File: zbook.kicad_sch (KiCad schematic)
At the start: 0 parts

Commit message: chore: adds new sheet and removes .lck
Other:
- sheet Peripherals renamed Peripherals 1
- added sheet Peripherals 2 (peripherals2.kicad_sch)
- sheet Peripherals 1: file peripherals.kicad_sch -> peripherals1.kicad_sch
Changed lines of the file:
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@@
 			(color 0 0 0 0.0000)
 		)
-		(property "Sheetname" "Peripherals"
+		(property "Sheetname" "Peripherals 1"
 			(at 138.43 56.4384 0)
 			(effects
@@
 			)
 		)
-		(property "Sheetfile" "peripherals.kicad_sch"
+		(property "Sheetfile" "peripherals1.kicad_sch"
 			(at 138.43 79.3246 0)
 			(effects
@@
 				)
 			)
+		)
+	)
+	(sheet
+		(at 189.23 58.42)
+		(size 19.05 19.05)
+		(exclude_from_sim no)
+		(in_bom yes)
+		(on_board yes)
+		(dnp no)
+		(fields_autoplaced yes)
+		(stroke
+			(width 0.1524)
+			(type solid)
+		)
+		(fill
+			(color 0 0 0 0.0000)
+		)
+		(property "Sheetname" "Peripherals 2"
+			(at 189.23 57.7084 0)
+			(effects
+				(font
+					(size 1.27 1.27)
+				)
+				(justify left bottom)
+			)
+		)
+		(property "Sheetfile" "peripherals2.kicad_sch"
+			(at 189.23 78.0546 0)
+			(effects
+				(font
+					(size 1.27 1.27)
+				)
+				(justify left top)
+			)
+		)
+		(instances
+			(project "zbook"
+				(path "/b90666d0-8852-4bb1-832d-f9d855027372"
+					(page "5")
+				)
+			)

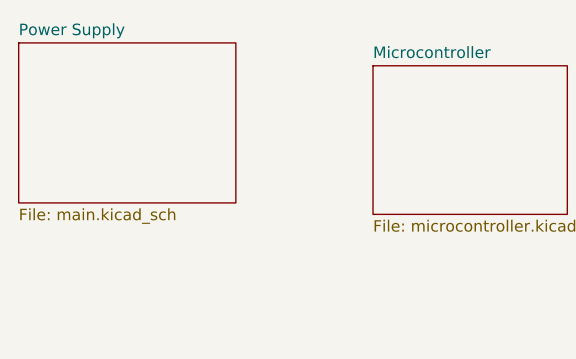
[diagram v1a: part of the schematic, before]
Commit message: refac: changes resistor symbol to US pattern, adds second USB-C connector
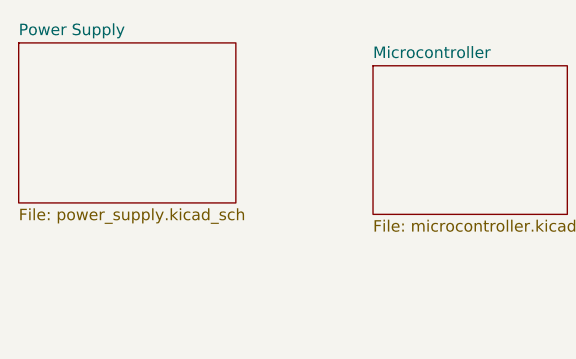
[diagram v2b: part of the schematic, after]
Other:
- sheet Power Supply: file main.kicad_sch -> power_supply.kicad_sch
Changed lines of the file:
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@@
 			)
 		)
-		(property "Sheetfile" "main.kicad_sch"
+		(property "Sheetfile" "power_supply.kicad_sch"
 			(at 44.45 66.6246 0)
 			(effects

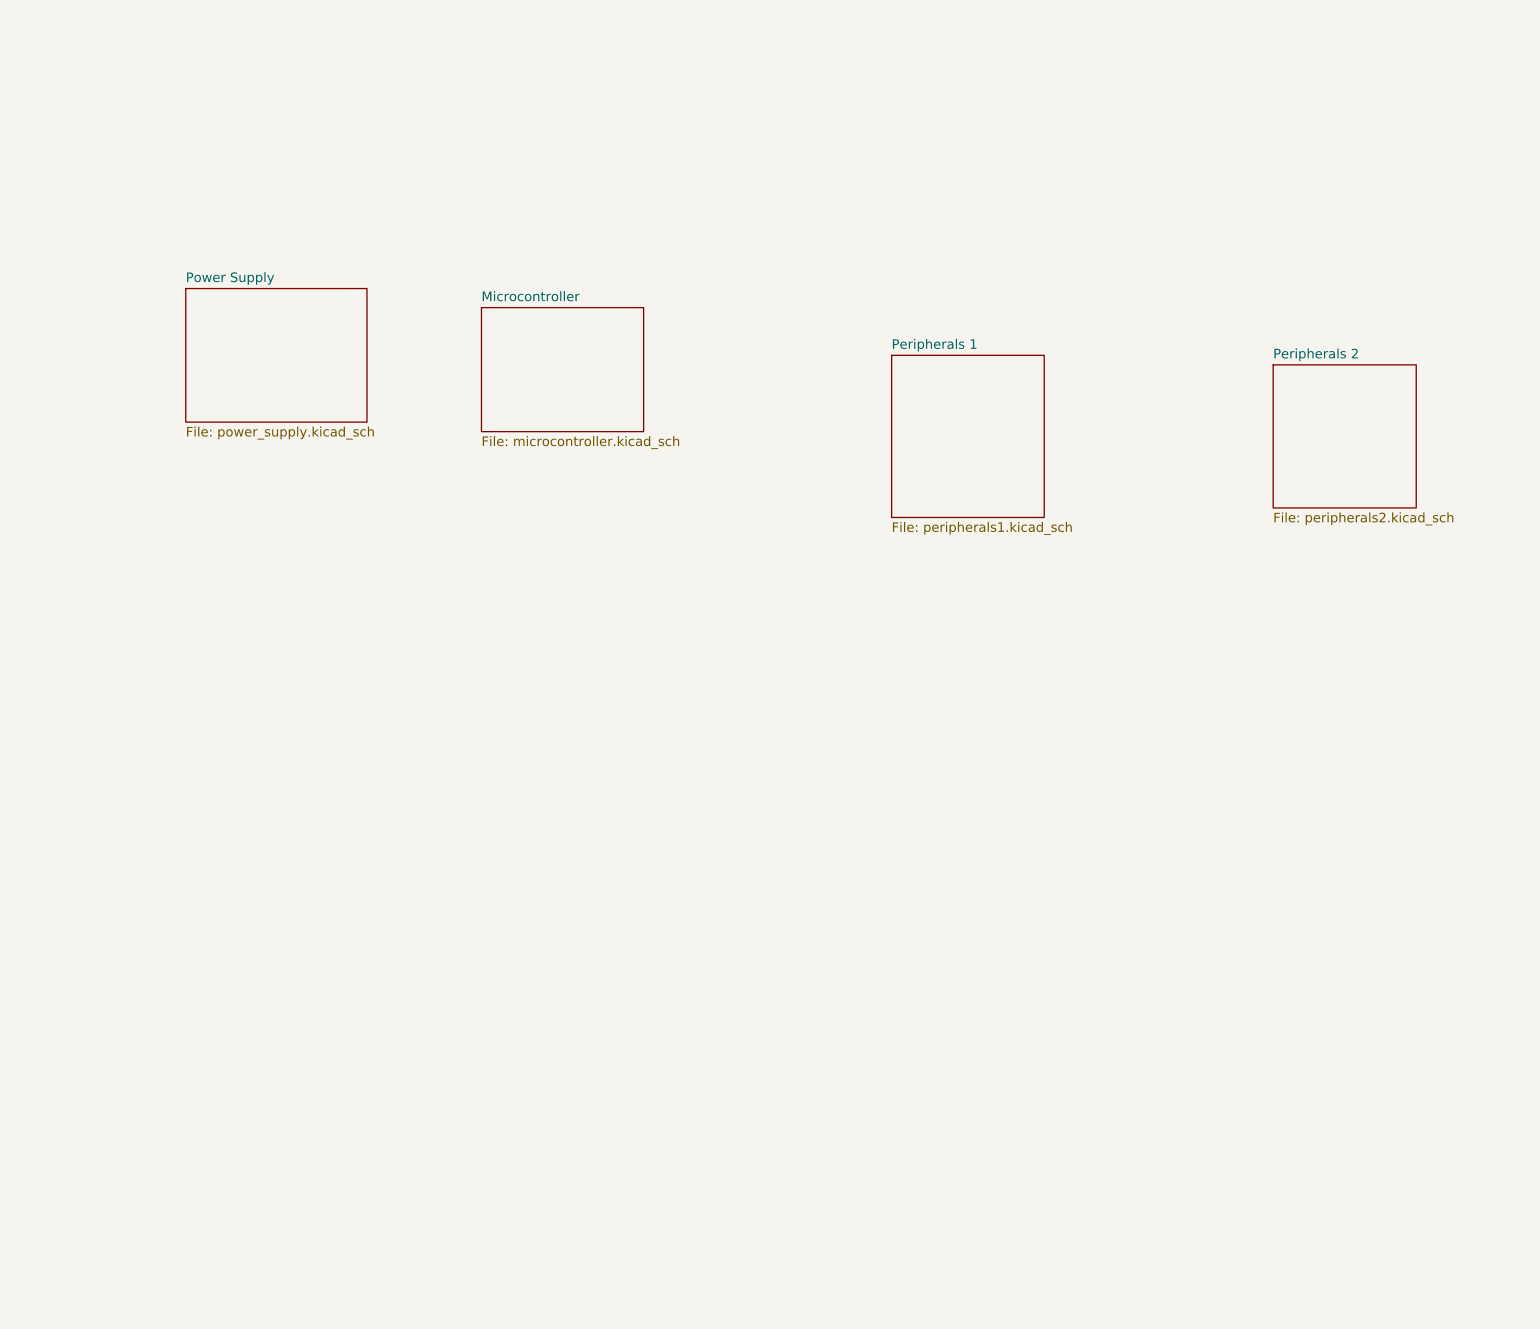
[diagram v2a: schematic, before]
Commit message: chore: adds titles to sheets and organizes root
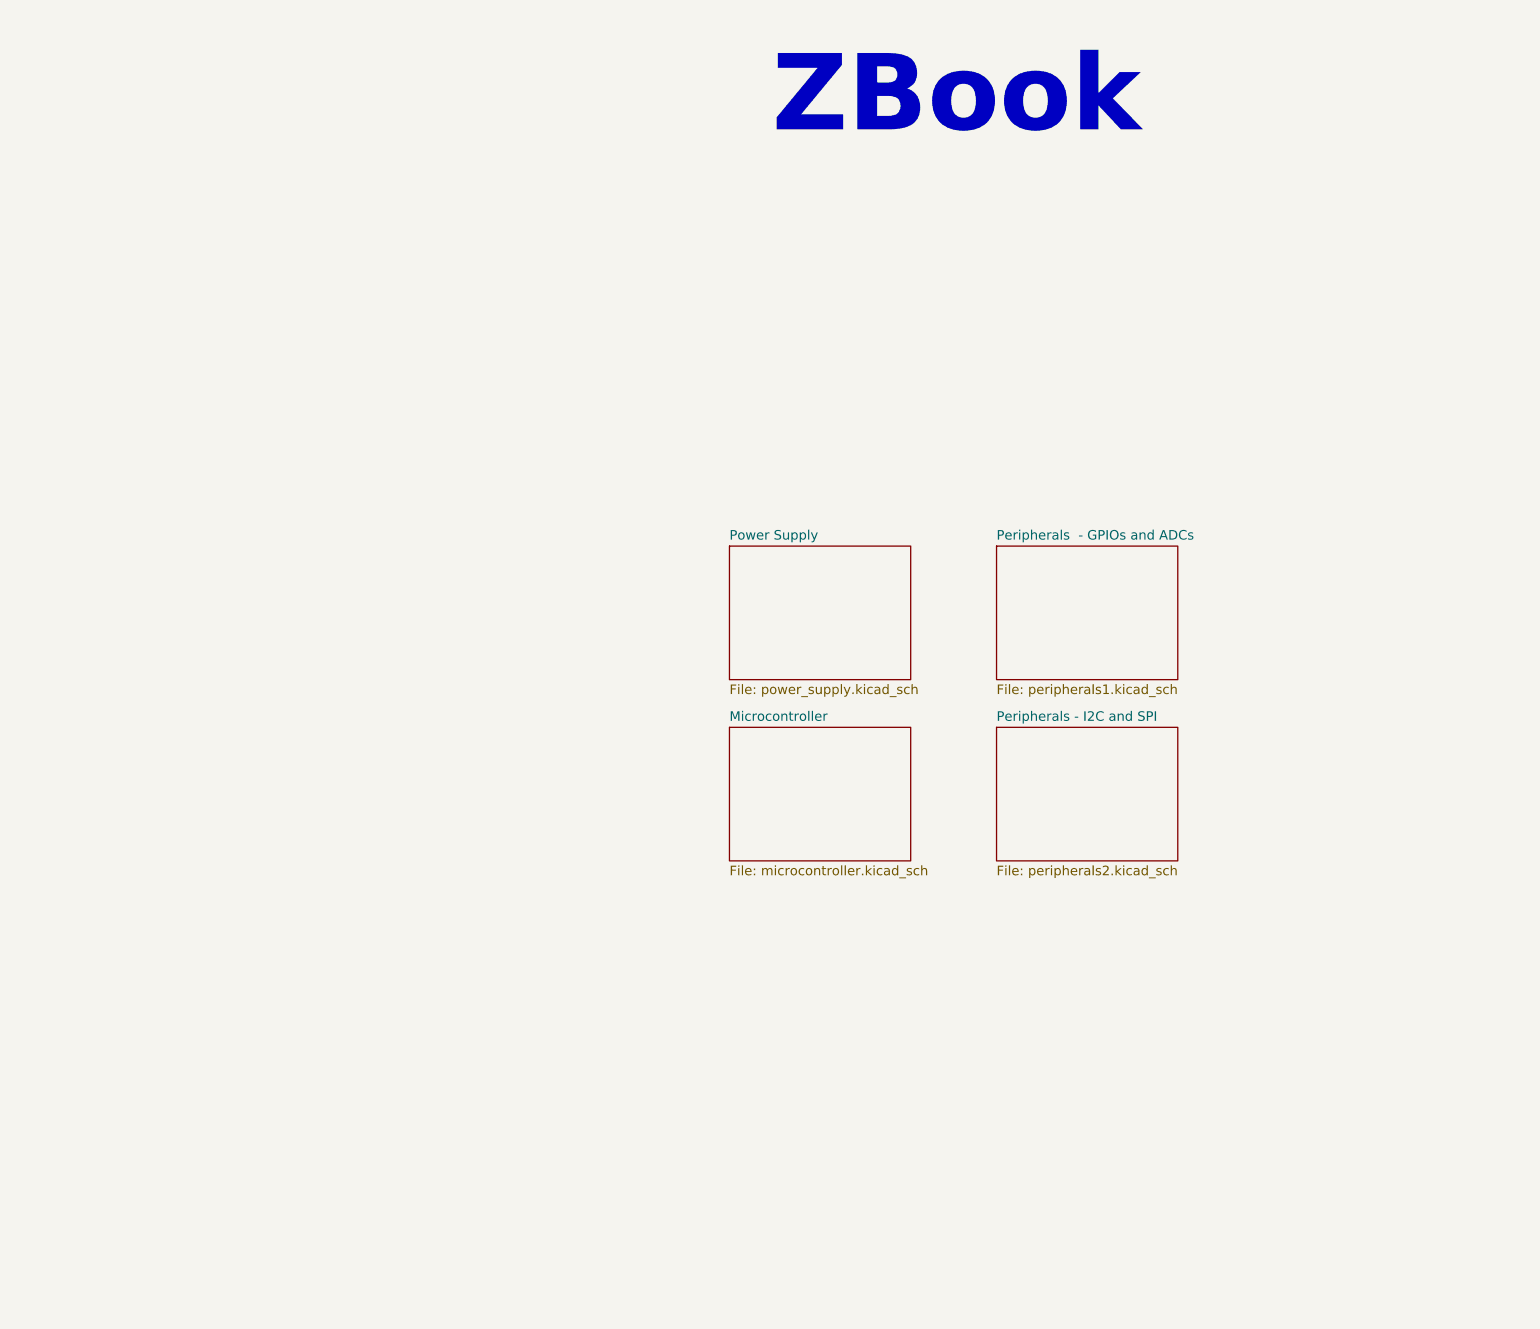
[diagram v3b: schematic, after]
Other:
- sheet Peripherals 1 renamed Peripherals  - GPIOs and ADCs
- sheet Peripherals 2 renamed Peripherals - I2C and SPI
- note added: "ZBook"
- company: (none) -> Os Circuitados
- title: (none) -> ZBook
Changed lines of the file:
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@@
 	(generator "eeschema")
 	(generator_version "9.0")
-	(paper "A3")
+	(paper "A4")
+	(title_block
+		(title "ZBook")
+		(company "Os Circuitados")
+	)
+	(text "ZBook\n"
+		(exclude_from_sim no)
+		(at 147.066 22.606 0)
+		(effects
+			(font
+				(size 10.16 10.16)
+				(thickness 2.032)
+				(bold yes)
+			)
+		)
+	)
 	(sheet
-		(at 138.43 57.15)
-		(size 20.32 21.59)
+		(at 152.4 82.55)
+		(size 24.13 17.78)
 		(exclude_from_sim no)
 		(in_bom yes)
@@
 			(color 0 0 0 0.0000)
 		)
-		(property "Sheetname" "Peripherals 1"
-			(at 138.43 56.4384 0)
+		(property "Sheetname" "Peripherals  - GPIOs and ADCs"
+			(at 152.4 81.8384 0)
 			(effects
 				(font
@@
 		)
 		(property "Sheetfile" "peripherals1.kicad_sch"
-			(at 138.43 79.3246 0)
+			(at 152.4 100.9146 0)
 			(effects
 				(font
@@
 	)
 	(sheet
-		(at 83.82 50.8)
-		(size 21.59 16.51)
+		(at 116.84 106.68)
+		(size 24.13 17.78)
 		(exclude_from_sim no)
 		(in_bom yes)
@@
 		)
 		(property "Sheetname" "Microcontroller"
-			(at 83.82 50.0884 0)
+			(at 116.84 105.9684 0)
 			(effects
 				(font
@@
 		)
 		(property "Sheetfile" "microcontroller.kicad_sch"
-			(at 83.82 67.8946 0)
+			(at 116.84 125.0446 0)
 			(effects
 				(font
@@
 	)
 	(sheet
-		(at 44.45 48.26)
+		(at 116.84 82.55)
 		(size 24.13 17.78)
 		(exclude_from_sim no)
@@
 		)
 		(property "Sheetname" "Power Supply"
-			(at 44.45 47.5484 0)
+			(at 116.84 81.8384 0)
 			(effects
 				(font
@@
 		)
 		(property "Sheetfile" "power_supply.kicad_sch"
-			(at 44.45 66.6246 0)
+			(at 116.84 100.9146 0)
 			(effects
 				(font
@@
 	)
 	(sheet
-		(at 189.23 58.42)
-		(size 19.05 19.05)
+		(at 152.4 106.68)
+		(size 24.13 17.78)
 		(exclude_from_sim no)
 		(in_bom yes)
@@
 			(color 0 0 0 0.0000)
 		)
-		(property "Sheetname" "Peripherals 2"
-			(at 189.23 57.7084 0)
+		(property "Sheetname" "Peripherals - I2C and SPI"
+			(at 152.4 105.9684 0)
 			(effects
 				(font
@@
 		)
 		(property "Sheetfile" "peripherals2.kicad_sch"
-			(at 189.23 78.0546 0)
+			(at 152.4 125.0446 0)
 			(effects
 				(font

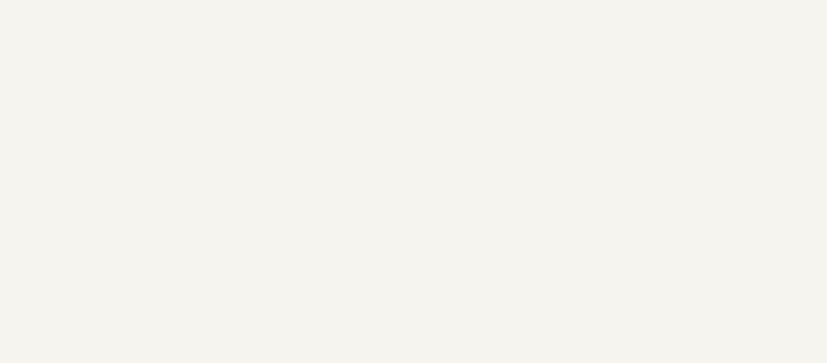
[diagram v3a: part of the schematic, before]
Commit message: feat:  adds requested components
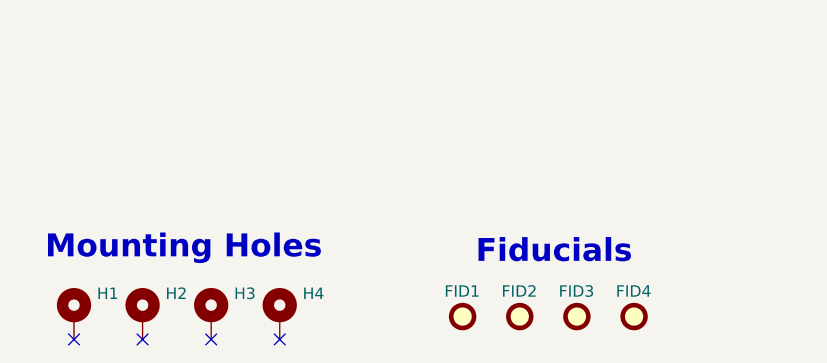
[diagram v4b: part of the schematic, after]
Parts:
- added FID1, FID2, FID3, FID4: Fiducial, Fiducial:Fiducial_0.5mm_Mask1.5mm, symbol Mechanical:Fiducial
- added H1, H2, H3, H4: MountingHole_Pad, MountingHole:MountingHole_2.5mm_Pad_Via, symbol Mechanical:MountingHole_Pad
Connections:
- no-connect marks 0 -> 4
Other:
- note added: "Fiducials"
- note added: "Mounting Holes"

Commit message: fix: fixes fiducials and mouting holes
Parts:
- FID1, FID2, FID3, FID4: footprint Fiducial:Fiducial_0.5mm_Mask1.5mm -> Fiducial:Fiducial_1mm_Mask3mm
- H1, H2, H3, H4: footprint MountingHole:MountingHole_2.5mm_Pad_Via -> MountingHole:MountingHole_3.2mm_M3
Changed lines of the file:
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@@
 			)
 		)
-		(property "Footprint" "Fiducial:Fiducial_0.5mm_Mask1.5mm"
+		(property "Footprint" "Fiducial:Fiducial_1mm_Mask3mm"
 			(at 90.17 181.61 0)
 			(effects
@@
 			)
 		)
-		(property "Footprint" "Fiducial:Fiducial_0.5mm_Mask1.5mm"
+		(property "Footprint" "Fiducial:Fiducial_1mm_Mask3mm"
 			(at 71.12 181.61 0)
 			(effects
@@
 			)
 		)
-		(property "Footprint" "Fiducial:Fiducial_0.5mm_Mask1.5mm"
+		(property "Footprint" "Fiducial:Fiducial_1mm_Mask3mm"
 			(at 83.82 181.61 0)
 			(effects
@@
 			)
 		)
-		(property "Footprint" "MountingHole:MountingHole_2.5mm_Pad_Via"
+		(property "Footprint" "MountingHole:MountingHole_3.2mm_M3"
 			(at 35.56 181.61 0)
 			(effects
@@
 			)
 		)
-		(property "Footprint" "Fiducial:Fiducial_0.5mm_Mask1.5mm"
+		(property "Footprint" "Fiducial:Fiducial_1mm_Mask3mm"
 			(at 77.47 181.61 0)
 			(effects
@@
 			)
 		)
-		(property "Footprint" "MountingHole:MountingHole_2.5mm_Pad_Via"
+		(property "Footprint" "MountingHole:MountingHole_3.2mm_M3"
 			(at 50.8 181.61 0)
 			(effects
@@
 			)
 		)
-		(property "Footprint" "MountingHole:MountingHole_2.5mm_Pad_Via"
+		(property "Footprint" "MountingHole:MountingHole_3.2mm_M3"
 			(at 43.18 181.61 0)
 			(effects
@@
 			)
 		)
-		(property "Footprint" "MountingHole:MountingHole_2.5mm_Pad_Via"
+		(property "Footprint" "MountingHole:MountingHole_3.2mm_M3"
 			(at 27.94 181.61 0)
 			(effects

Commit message: feat: adds additional mounting hole
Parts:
- added H5: MountingHole_Pad, MountingHole:MountingHole_3.2mm_M3, symbol Mechanical:MountingHole_Pad
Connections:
- no-connect marks 4 -> 5
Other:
- moved on the sheet: H1, H2, H3, H4
